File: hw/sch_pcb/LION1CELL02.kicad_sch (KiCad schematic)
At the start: 82 parts, among them IC1 BQ294602DRVR, J1 CONN1_1, J10 JUMP_2x1, J11 JUMP_2x1, J12 JUMP_2x1, J13 JUMP_2x1, J2 CONN1_1, J3 Jack-DC, J4 JUMP_2x1, J5 JUMP_2x1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

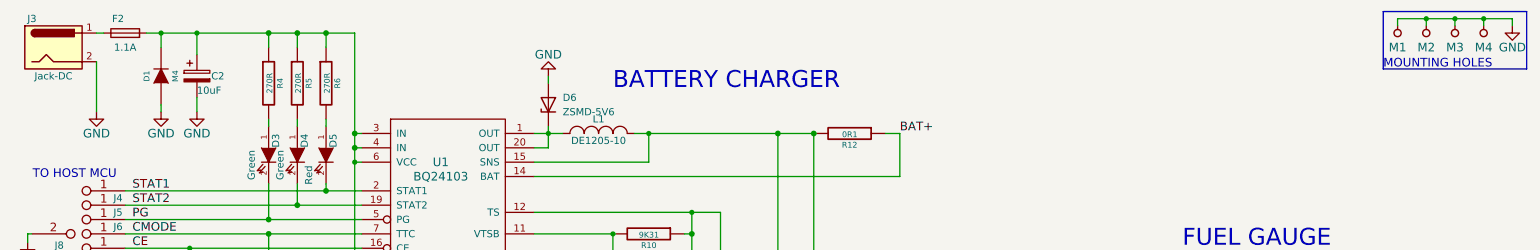
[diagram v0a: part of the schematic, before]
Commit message: Update kicad project to version 8.
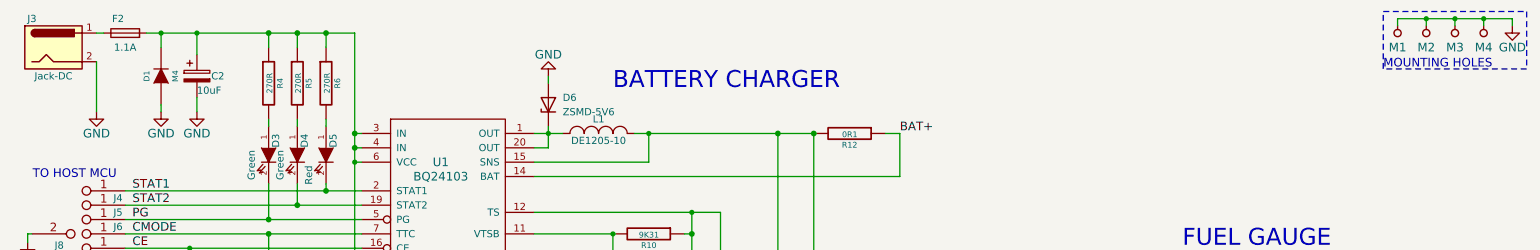
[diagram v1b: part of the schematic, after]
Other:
- company: (none) -> Mlab.cz
- title: (none) -> LION1CELL02A
